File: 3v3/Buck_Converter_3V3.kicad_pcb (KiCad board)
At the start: 2 copper layers, 14.8 x 39 mm, 12 parts, among them P1 CONN_2, P2 CONN_2, U1 LM2597

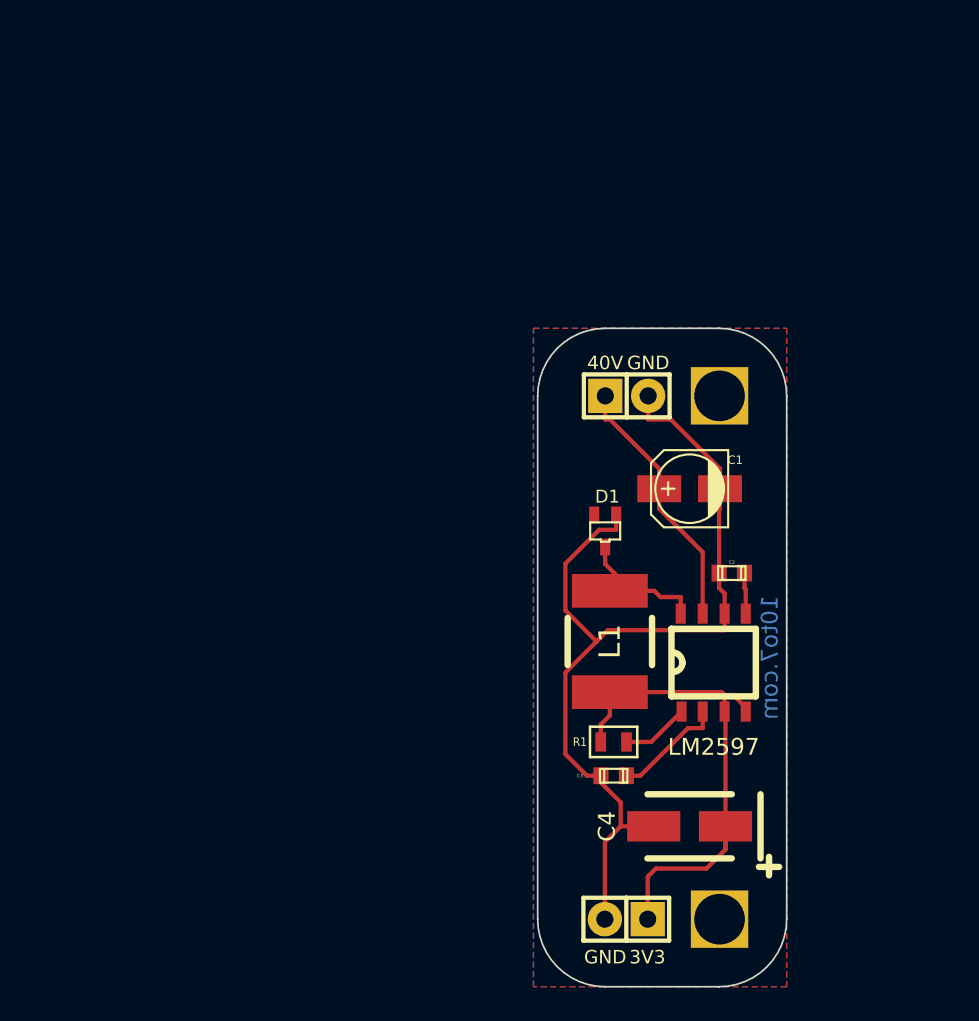
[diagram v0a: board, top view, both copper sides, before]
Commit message: updated to add a fuse and led
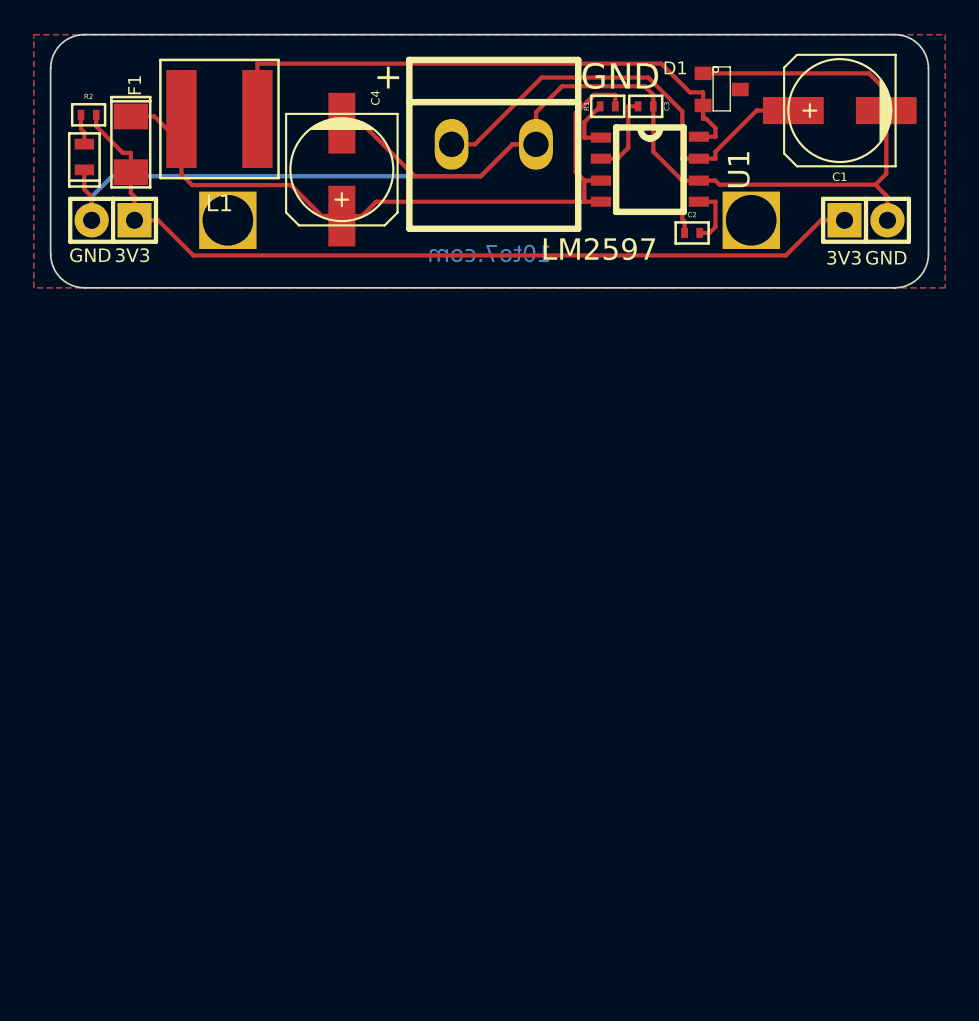
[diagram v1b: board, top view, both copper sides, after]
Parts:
- added D2: Power, 10to7_sm_standard:SM0603_Polarity, F.Cu at (121.9, 86.8)
- added F1: 500MA, 10to7_sm_standard:SM1206POL, F.Cu at (124.6, 86.1)
- added R2: 100, 10to7_sm_standard:SM0402, F.Cu at (122.1, 84.3)
- added VIn1: CONN_2, 10to7_connectors:2_Pin_Screw_5mm_Pitch, F.Cu at (146.1, 86.1)
- C1: footprint Capacitors_SMD:c_elec_4x4.5 -> Capacitors_SMD:c_elec_6.3x4.5
- C2, C3: footprint Capacitors_SMD:c_0603 -> 10to7_sm_standard:SM0402
- C4: footprint Capacitors_Tantalum_SMD:TantalC_SizeB_EIA-3528_HandSoldering -> Capacitors_SMD:c_elec_6.3x7.7
- D1: value DIODESCH -> HSMS-2800; footprint SMD_Packages:SOT323 -> SMD_Packages:SOT23
- L1: value 100uH -> 300uH; footprint Inductors_NEOSID:Neosid_Inductor_SM-NE56_SMD2220 -> 10to7_sm_standard:6mmx6mm_inductor
- R1: footprint 10to7_sm_standard:SM0603 -> 10to7_sm_standard:SM0402
- moved P2 51.4 mm to (123.6, 90.6)
- moved C4 44.0 mm to (137.1, 87.6), turned to 270 degrees
- moved 3mmHole_1 41.4 mm to (162.4, 92.6)
- moved C3 39.7 mm to (155.1, 83.8)
- moved L1 38.6 mm to (129.9, 84.6), turned to 180 degrees
- moved R1 37.7 mm to (152.9, 83.8), turned to 180 degrees
- moved 3mmHole 30.9 mm to (130.9, 86.6)
- moved U1 29.4 mm to (155.4, 87.6), turned to 270 degrees
- moved D1 27.0 mm to (159.6, 82.8), turned to 270 degrees
- moved C1 24.1 mm to (166.6, 84.1)
- moved C2 20.3 mm to (157.9, 91.3), turned to 180 degrees
- moved P1 17.6 mm to (168.2, 90.6)
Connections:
- C4 pad 1: +3.3V -> /Feedback
- L1 pad 2: +3.3V -> /Feedback
- P1 pad 1: +12V -> +3.3V
- R1 pad 1: +3.3V -> /Feedback
- U1 pad 3: +3.3V -> /Feedback
- U1 pad 4: +3.3V -> /Feedback
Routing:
- net /Feedback: track 0.00 -> 42.8 mm
- net GND: track 56.1 -> 95.4 mm
- net Net-(D1-Pad2): track 8.59 -> 34.4 mm
- net +3.3V: track 30.2 -> 51.3 mm
- net +12V: track 15.4 -> 26.9 mm
- net Net-(D2-Pad1): track 0.00 -> 1.82 mm
- net Net-(C3-Pad1): track 6.67 -> 4.93 mm
- net /Shutdown_Soft-start: track 2.43 -> 3.56 mm
- net /Error_Flag: track 4.01 -> 3.22 mm
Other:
- board size 14.8 x 39 mm -> 52 x 15 mm
- net class Default: clearance 0.254 -> 0
- rule trace_clearance: 0.254 -> 0
- board text added: "+"
- board text removed: "40V"
